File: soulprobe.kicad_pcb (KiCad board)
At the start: 4 copper layers, 44 x 44 mm, 83 parts, among them J1 JTAG, J2 UART_PROG, J3 Micro_SD_Card_Det_Hirose_DM3AT, J4 USB_MAIN, J5 USB_DBG, SW1 BOOT, SW2 RST, U1 ESP32-P4, U3 TLV62569DBV, U4 AP7361C-33E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

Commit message: Rev 1
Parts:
- removed ? (x8): , 
- removed C37, C41: 10uF, Capacitor_SMD:C_0402_1005Metric
- removed C39, C40, C42: 0.1uF, Capacitor_SMD:C_0402_1005Metric
- removed JP1: 3V3PWR, Jumper:SolderJumper-2_P1.3mm_Bridged_Pad1.0x1.5mm
- removed JP2: VBAT, Jumper:SolderJumper-2_P1.3mm_Bridged_Pad1.0x1.5mm
- removed R12, R13, R14, R15, R16, R17, R18, R19: 10k, Resistor_SMD:R_0402_1005Metric
- removed R20, R4: 5.11k, Resistor_SMD:R_0402_1005Metric
- removed R21, R22: 0R, Resistor_SMD:R_0402_1005Metric
- removed R5, R6: 22R, Resistor_SMD:R_0402_1005Metric
- removed SW1: BOOT, Button_Switch_SMD:SW_Push_1P1T_XKB_TS-1187A
- removed SW2: RST, Button_Switch_SMD:SW_Push_1P1T_XKB_TS-1187A
- removed U4: AP7361C-33E, Package_TO_SOT_SMD:SOT-223-3_TabPin2
- removed U5: W25Q128JVE, Package_SON:WSON-8-1EP_8x6mm_P1.27mm_EP3.4x4.3mm
- added H1: Mount, MountingHole:MountingHole_2.2mm_M2_Pad, F.Cu at (106.5, 136.0)
- added H2: Mount, MountingHole:MountingHole_2.2mm_M2_Pad, F.Cu at (106.5, 104.0)
- added H3: Mount, MountingHole:MountingHole_2.2mm_M2_Pad, F.Cu at (143.5, 136.0)
- added H4: Mount, MountingHole:MountingHole_2.2mm_M2_Pad, F.Cu at (143.5, 104.0)
- added REF**: OSHW-Logo2_7.3x6mm_SilkScreen, Symbol:OSHW-Logo2_7.3x6mm_SilkScreen, F.Cu at (143.0, 111.8)
- added U2: W25Q128JVS, Package_SO:SOIC-8_5.3x5.3mm_P1.27mm, F.Cu at (121.9, 136.4)
- J1: value JTAG -> PROG_PIN; footprint Connector_PinHeader_2.54mm:PinHeader_2x10_P2.54mm_Vertical -> Connector_PinHeader_1.27mm:PinHeader_2x10_P1.27mm_Vertical_SMD; moved to B.Cu
- J2: footprint Connector_PinHeader_2.54mm:PinHeader_1x06_P2.54mm_Vertical -> Connector_PinHeader_1.27mm:PinHeader_1x06_P1.27mm_Vertical; moved to B.Cu
- J3: value Micro_SD_Card_Det_Hirose_DM3AT -> DBG_PINS; footprint Connector_Card:microSD_HC_Hirose_DM3AT-SF-PEJM5 -> Connector_PinHeader_1.27mm:PinHeader_2x10_P1.27mm_Vertical_SMD; moved to B.Cu
- J4: value USB_MAIN -> SD_PINS; footprint Connector_USB:USB_C_Receptacle_HRO_TYPE-C-31-M-12 -> Connector_PinHeader_1.27mm:PinHeader_2x10_P1.27mm_Vertical_SMD; moved to B.Cu
- J5: moved to B.Cu
- moved J1 138.0 mm to (107.5, 120.0), turned to 180 degrees
- moved U1 104.5 mm to (125.4, 123.8), turned to 0 degrees
- moved J4 82.9 mm to (125.0, 105.0), turned to 90 degrees
- moved C38 74.0 mm to (116.2, 138.0), turned to 90 degrees
- moved R11 72.6 mm to (119.9, 132.9), turned to 180 degrees
- moved C34 66.7 mm to (135.2, 135.1), turned to 180 degrees
- moved C32 65.8 mm to (132.0, 129.5)
- moved Y2 65.6 mm to (115.5, 118.0), turned to 90 degrees
- moved C33 64.8 mm to (132.0, 130.4)
- moved C28 63.0 mm to (116.4, 127.2), turned to 180 degrees
- moved C25 62.4 mm to (113.7, 119.1), turned to 90 degrees
- moved C30 61.5 mm to (119.9, 131.2), turned to 180 degrees
- moved C29 61.2 mm to (119.2, 128.6), turned to -90 degrees
- moved J5 60.9 mm to (136.1, 133.3)
- moved C20 60.4 mm to (115.2, 123.2), turned to 180 degrees
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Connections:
- C11 pad 1: Net-(JP2-B) -> +3V3
- C12 pad 1: Net-(JP2-B) -> +3V3
- J1 pad 1: unconnected-(J1-Pin_1-Pad1) -> +3V3
- J1 pad 10: GND -> IO12
- J1 pad 13: IO9/nRST -> GND
- J1 pad 14: IO12 -> IO13
- J1 pad 15: IO10/TDO -> IO9/nRST
- J1 pad 16: IO13 -> GND
- J1 pad 17: IO11/nRST -> IO10/TDO
- J1 pad 19: +5V -> IO11/nRST
- J1 pad 6: GND -> IO2
- J1 pad 7: Net-(J1-Pin_7) -> IO6/SWDIO
- J1 pad 8: GND -> IO3
- J1 pad 9: Net-(J1-Pin_9) -> IO7/SWCLK
- J3 pad 1: IO41/SDDAT2 -> +3V3
- J3 pad 10: GND -> JTAG_D+
- J3 pad 11: GND -> IO38/U0RXD
- J3 pad 2: IO42/SDDAT3 -> +3V3
- J3 pad 3: IO44/SDCMD -> +3V3
- J3 pad 5: IO43/SDCLK -> CHIP_PU
- J3 pad 6: GND -> IO27
- J3 pad 7: IO39/SDDAT0 -> IO35/BOOT
- J3 pad 8: IO40/SDDAT1 -> IO26
- J3 pad 9: IO45/SDDET -> GND
- J5 pad 1: +5V -> +3V3
- J5 pad 2: IO24/JTAG_DM -> JTAG_D-
- J5 pad 3: IO25/JTAG_DP -> JTAG_D+
- U1 pad 102: Net-(JP2-B) -> +3V3
- U1 pad 2: unconnected-(U1-GPIO2/ADC-Pad2) -> IO2
- U1 pad 3: unconnected-(U1-GPIO3/ADC-Pad3) -> IO3
- U1 pad 49: USB_DM -> USB_D-
- U1 pad 50: USB_DP -> USB_D+
- U1 pad 52: IO24/JTAG_DM -> JTAG_D-
- U1 pad 53: IO25/JTAG_DP -> JTAG_D+
- U1 pad 55: unconnected-(U1-GPIO26/ADC/USB-Pad55) -> IO26
- U1 pad 56: unconnected-(U1-GPIO27/ADC/USB-Pad56) -> IO27
- U1 pad 88: unconnected-(U1-GPIO46-Pad88) -> IO46
- U1 pad 89: unconnected-(U1-GPIO47-Pad89) -> IO47
- U1 pad 90: unconnected-(U1-GPIO48-Pad90) -> IO48
- U1 pad 92: unconnected-(U1-GPIO49/ADC-Pad92) -> IO49
- U1 pad 93: unconnected-(U1-GPIO50/ADC-Pad93) -> IO50
- U1 pad 94: unconnected-(U1-GPIO51/ADC-Pad94) -> IO51
- U1 pad 95: unconnected-(U1-GPIO52/ADC-Pad95) -> IO52
- U1 pad 97: unconnected-(U1-GPIO53/ADC-Pad97) -> IO53
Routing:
- net +3V3: track 0.00 -> 79.7 mm, vias 0 -> 22
- net CHIP_PU: track 0.00 -> 51.5 mm, vias 0 -> 4
- net +1V2: track 0.00 -> 45.9 mm, vias 0 -> 4
- net VDDO_FLASH: track 0.00 -> 38.0 mm, vias 0 -> 4
- net GND: track 0.00 -> 36.6 mm, vias 0 -> 78
- net IO35/BOOT: track 0.00 -> 35.5 mm, vias 0 -> 4
- net IO38/U0RXD: track 0.00 -> 27.5 mm, vias 0 -> 2
- net JTAG_D-: track 0.00 -> 24.9 mm, vias 0 -> 2
- net IO37/U0TXD: track 0.00 -> 24.9 mm, vias 0 -> 1
- net JTAG_D+: track 0.00 -> 24.4 mm, vias 0 -> 2
- net USB_D-: track 0.00 -> 19.6 mm, vias 0 -> 2
- net USB_D+: track 0.00 -> 19.1 mm, vias 0 -> 2
- net IO27: track 0.00 -> 17.9 mm, vias 0 -> 2
- net IO26: track 0.00 -> 17.9 mm, vias 0 -> 2
- net IO53: track 0.00 -> 17.7 mm, vias 0 -> 1
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- added copper zone on In2.Cu, net +3V3
- added copper zone on B.Cu, net GND
- added copper zone on F.Cu, net GND
- added copper zone on In1.Cu, net GND
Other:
- board size 44 x 44 mm -> 45 x 40 mm
- board text added: "SoulCore-ESP32P4 By Jackson M Hu Rev. 1 Dec 2025"

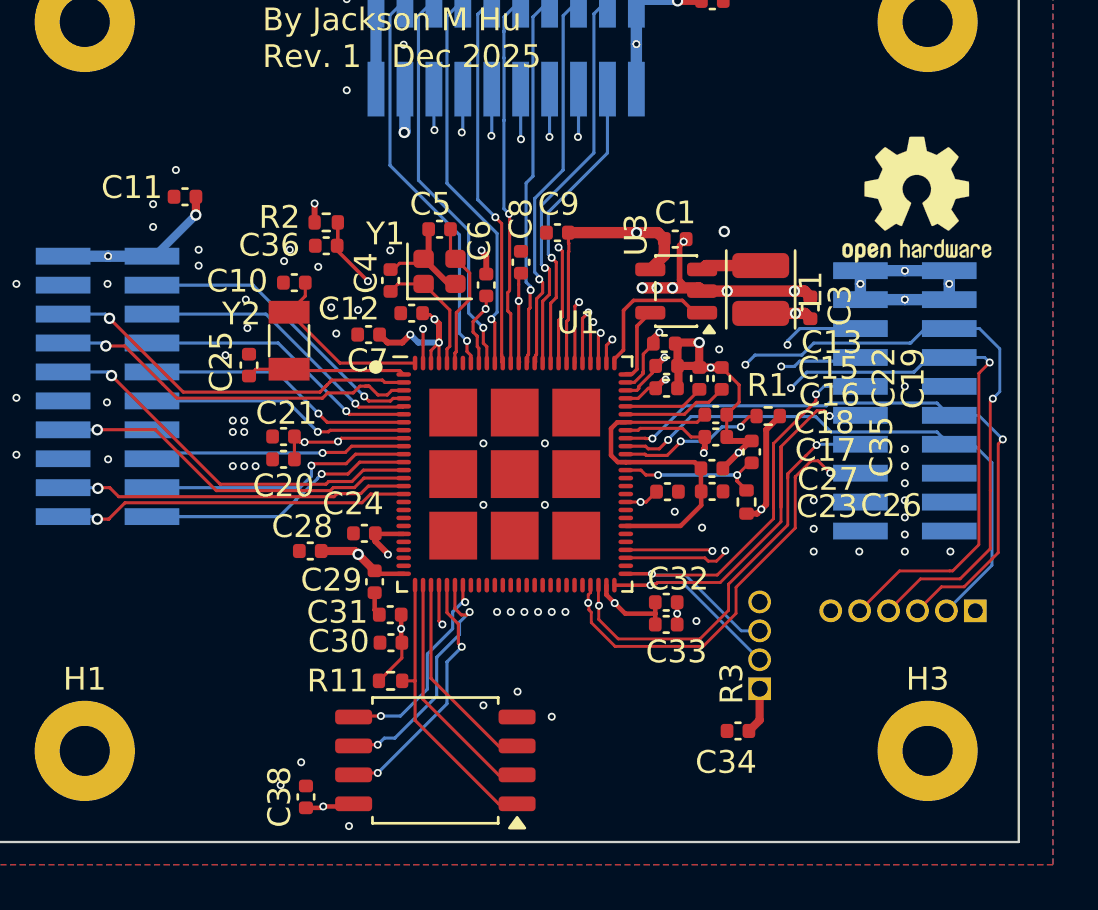
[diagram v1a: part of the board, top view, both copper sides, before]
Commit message: Rev 1 - rework traces
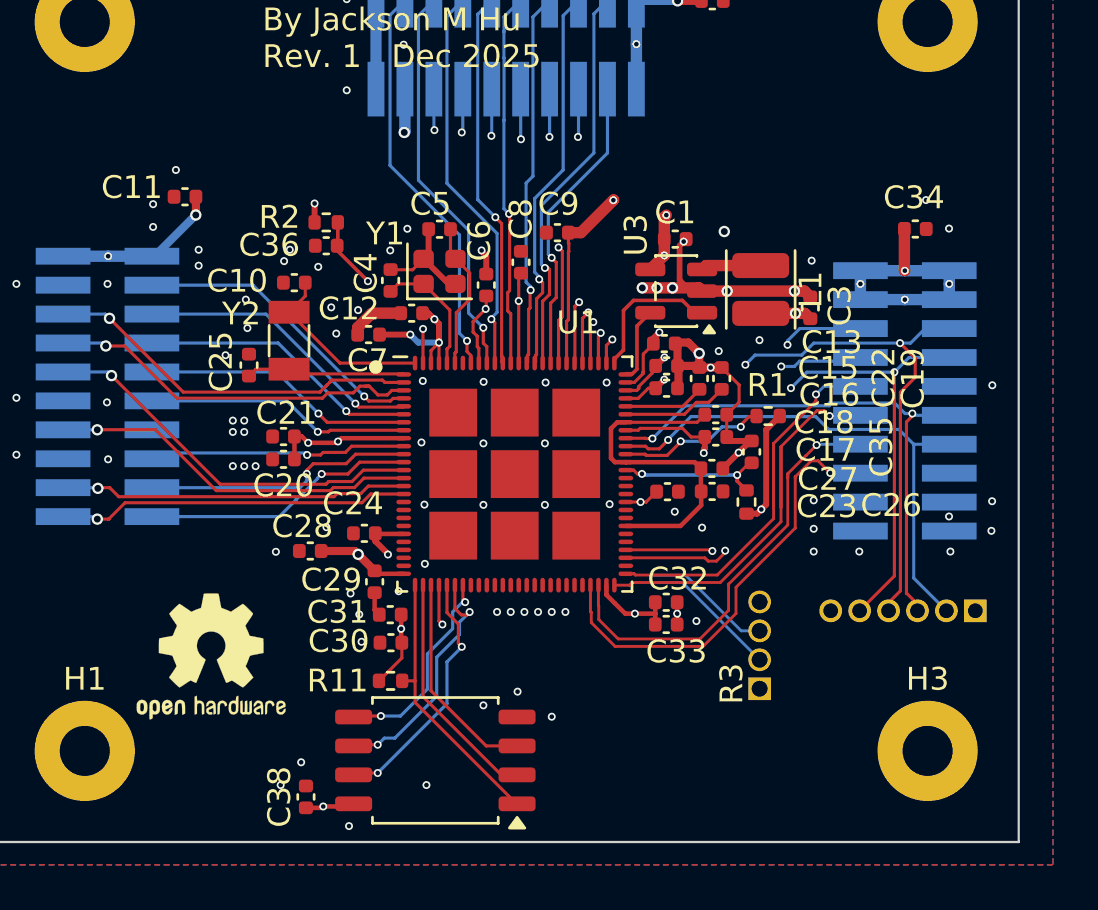
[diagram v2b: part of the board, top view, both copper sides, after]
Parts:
- moved REF** 36.9 mm to (112.0, 131.8)
- moved C34 23.4 mm to (143.0, 113.1), turned to 0 degrees
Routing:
- net IO35/BOOT: track 35.5 -> 30.2 mm
- net CHIP_PU: track 51.5 -> 46.5 mm
- net IO38/U0RXD: track 27.5 -> 24.1 mm
- net GND: track 36.6 -> 39.0 mm, vias 78 -> 94
- net IO37/U0TXD: track 24.9 -> 23.3 mm
- net +3V3: track 79.7 -> 78.6 mm, vias 22 -> 24
- net JTAG_D-: track 24.9 -> 24.6 mm, vias 2 -> 1
- net USB_D-: vias 2 -> 1
- net JTAG_D+: vias 2 -> 1
- net USB_D+: vias 2 -> 1
